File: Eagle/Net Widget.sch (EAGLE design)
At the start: 14 parts, among them IC1 ATmega1284P

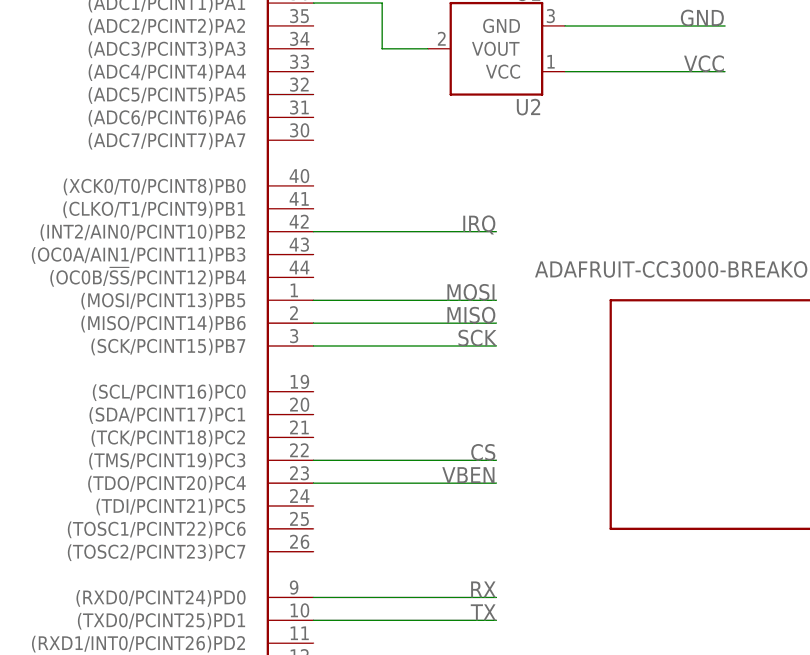
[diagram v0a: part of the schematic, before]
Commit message: Match CS and VBEN to Wicked Devices wildfire.
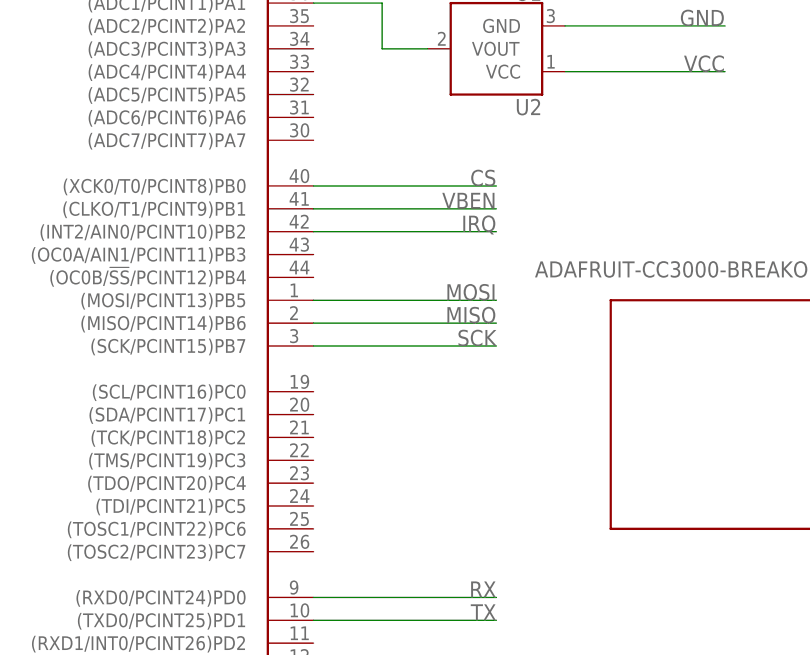
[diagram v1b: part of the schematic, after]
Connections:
- net CS: now also IC1.(XCK0/T0/PCINT8)PB0; no longer IC1.(TMS/PCINT19)PC3
- net VBEN: now also IC1.(CLKO/T1/PCINT9)PB1; no longer IC1.(TDO/PCINT20)PC4
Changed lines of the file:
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@@
 </segment>
 <segment>
-<pinref part="IC1" gate="G$1" pin="(TMS/PCINT19)PC3"/>
-<wire x1="83.82" y1="27.94" x2="104.14" y2="27.94" width="0.1524" layer="91"/>
-<label x="104.14" y="27.94" size="1.778" layer="95" rot="MR0"/>
+<pinref part="IC1" gate="G$1" pin="(XCK0/T0/PCINT8)PB0"/>
+<wire x1="83.82" y1="58.42" x2="104.14" y2="58.42" width="0.1524" layer="91"/>
+<label x="104.14" y="58.42" size="1.778" layer="95" rot="MR0"/>
 </segment>
 </net>
@@
 </segment>
 <segment>
-<pinref part="IC1" gate="G$1" pin="(TDO/PCINT20)PC4"/>
-<wire x1="83.82" y1="25.4" x2="104.14" y2="25.4" width="0.1524" layer="91"/>
-<label x="104.14" y="25.4" size="1.778" layer="95" rot="MR0"/>
+<pinref part="IC1" gate="G$1" pin="(CLKO/T1/PCINT9)PB1"/>
+<wire x1="83.82" y1="55.88" x2="104.14" y2="55.88" width="0.1524" layer="91"/>
+<label x="104.14" y="55.88" size="1.778" layer="95" rot="MR0"/>
 </segment>
 </net>

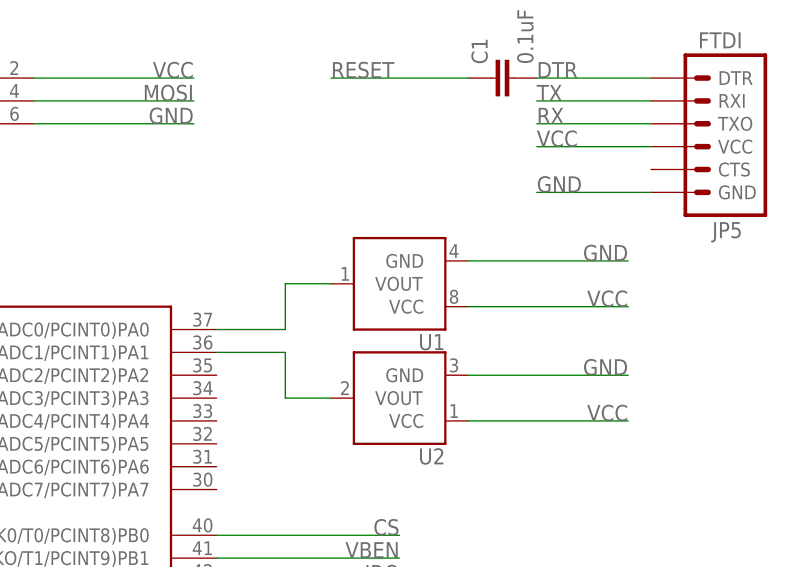
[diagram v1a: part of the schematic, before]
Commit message: Re-route w/ more space between pads and vias.
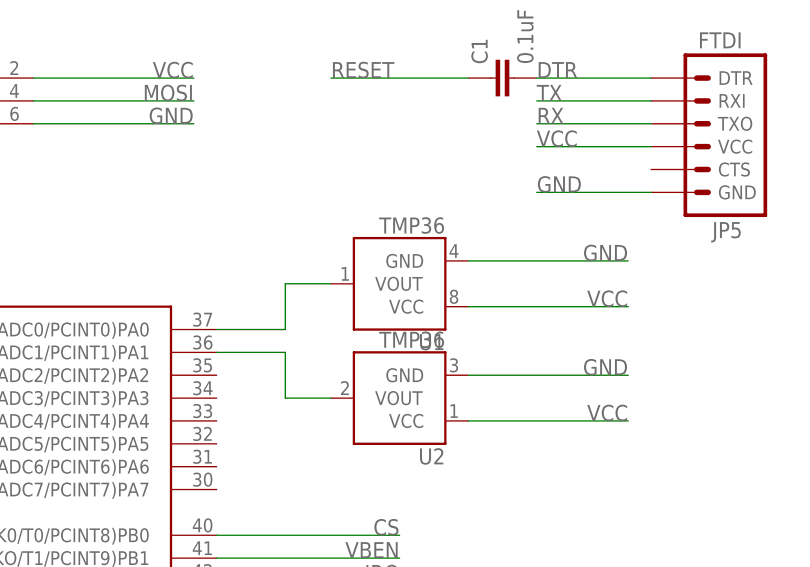
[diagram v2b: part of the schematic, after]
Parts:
- U1, U2: value (none) -> TMP36
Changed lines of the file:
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@@
 <part name="C1" library="rcl" deviceset="C-EU" device="C1206" value="0.1uF"/>
 <part name="CN1" library="Net Widget" deviceset="USB" device="PWR"/>
-<part name="U1" library="Net Widget" deviceset="TMP36" device=""/>
-<part name="U2" library="Net Widget" deviceset="TMP36" device="GT9"/>
+<part name="U1" library="Net Widget" deviceset="TMP36" device="" value="TMP36"/>
+<part name="U2" library="Net Widget" deviceset="TMP36" device="GT9" value="TMP36"/>
 </parts>
 <sheets>

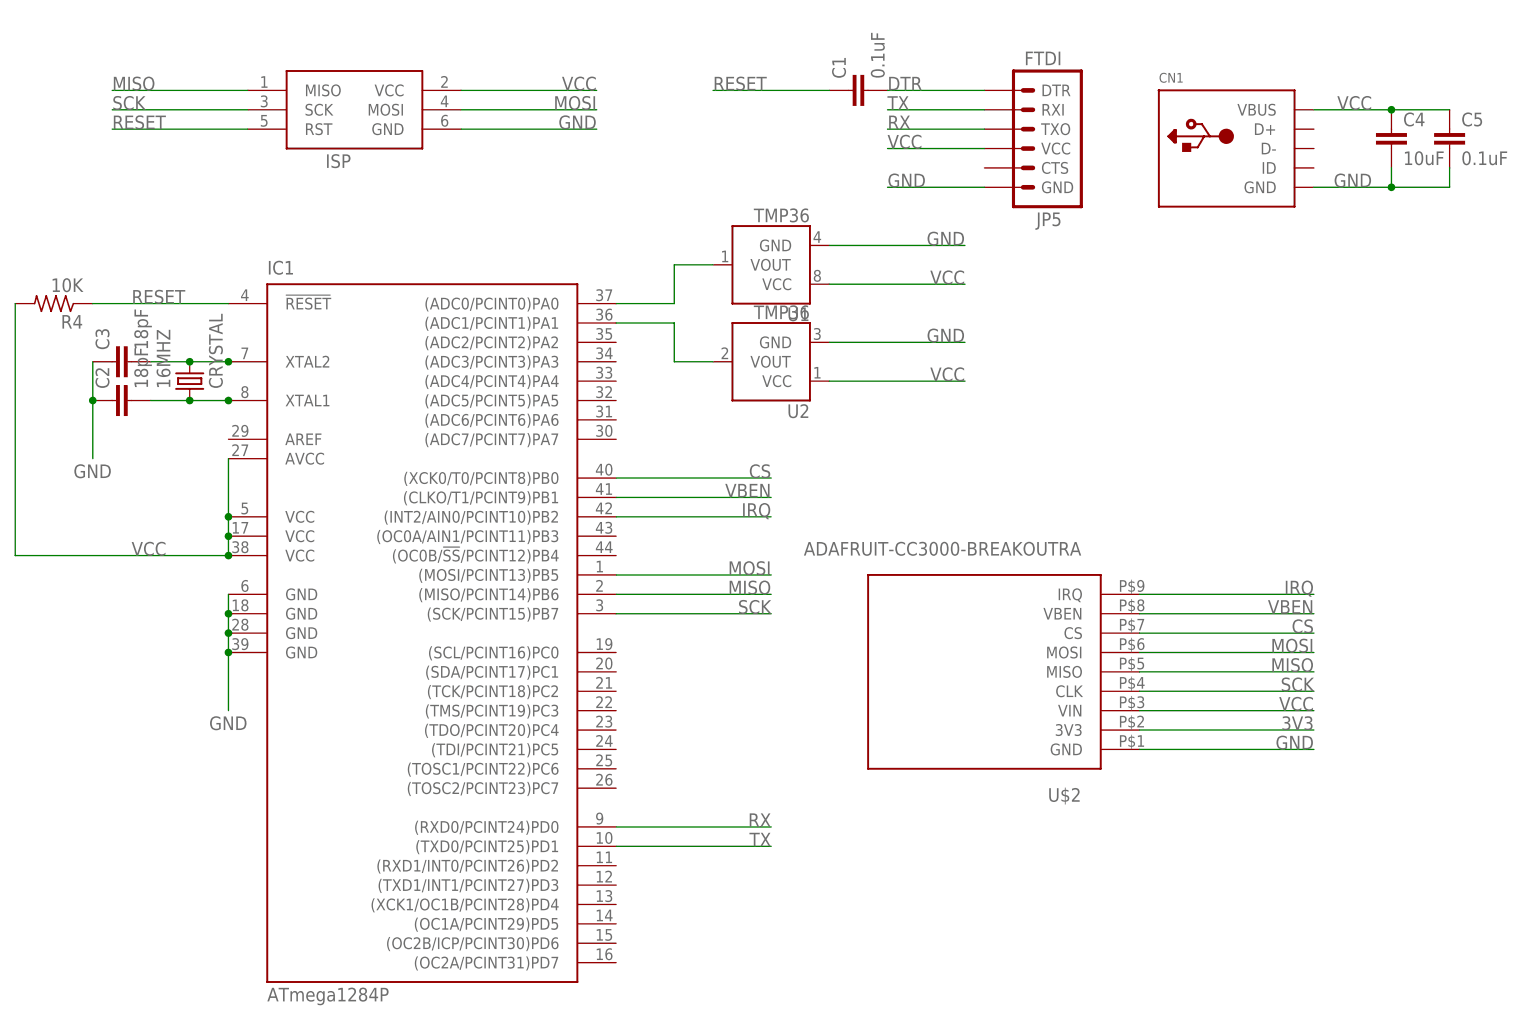
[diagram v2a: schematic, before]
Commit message: Remove temp sensor; add LEDs and touch.
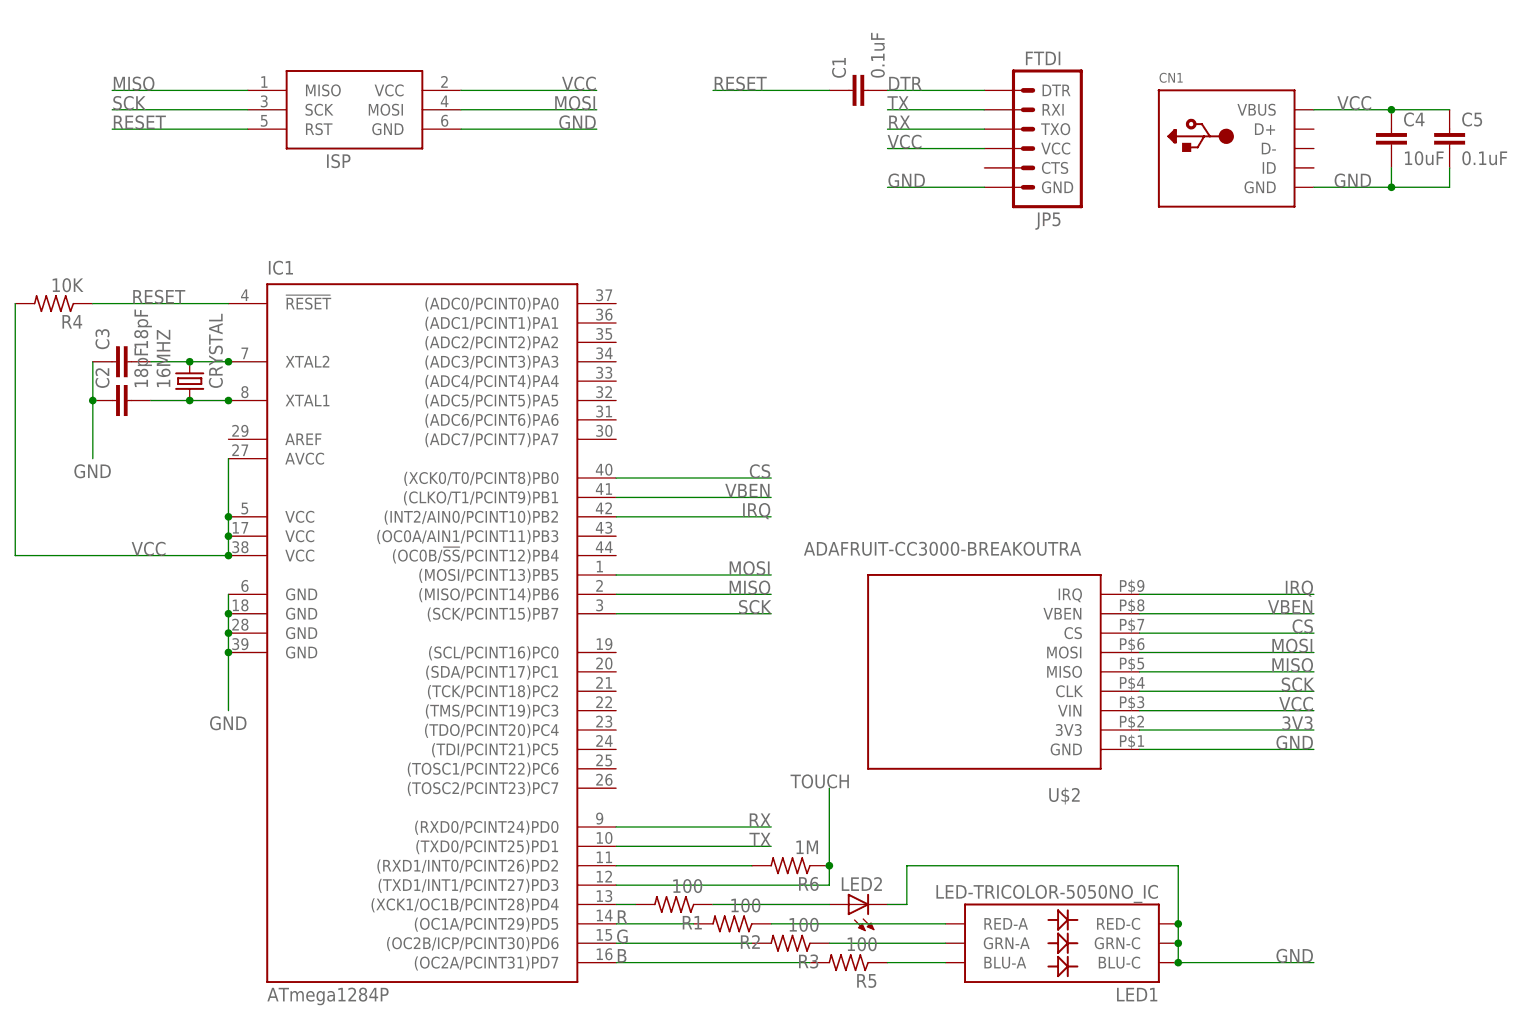
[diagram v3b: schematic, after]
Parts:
- removed U1: TMP36, Net Widget:TMP36
- removed U2: TMP36, Net Widget:TMP36GT9
- added LED1: LED-TRICOLOR-5050NO_IC, SparkFun-LED:LED-TRICOLOR-5050NO_IC
- added LED2: (no value), led:LEDSMT1206
- added R1, R2, R3, R5: 100, rcl:R-US_R1206
- added R6: 1M, rcl:R-US_R1206
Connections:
- removed net N$2: IC1.(ADC1/PCINT1)PA1, U2.VOUT
- new net B: IC1.(OC2A/PCINT31)PD7, R5.2
- new net G: IC1.(OC2B/ICP/PCINT30)PD6, R3.2
- new net N$10: LED1.RED-A, R2.1
- new net N$11: LED1.GRN-A, R3.1
- new net N$12: LED1.BLU-A, R5.1
- new net N$3: IC1.(XCK1/OC1B/PCINT28)PD4, R1.2
- new net N$9: LED2.A, R1.1
- new net R: IC1.(OC1A/PCINT29)PD5, R2.2
- new net TOUCH: IC1.(TXD1/INT1/PCINT27)PD3, R6.1
- net GND: now also LED1.BLU-C, LED1.GRN-C, LED1.RED-C, LED2.C; no longer U1.GND, U2.GND
- net N$1: now also IC1.(RXD1/INT0/PCINT26)PD2, R6.2; no longer IC1.(ADC0/PCINT0)PA0, U1.VOUT
- net VCC: no longer U1.VCC, U2.VCC
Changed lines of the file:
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@@
 <part name="C1" library="rcl" deviceset="C-EU" device="C1206" value="0.1uF"/>
 <part name="CN1" library="Net Widget" deviceset="USB" device="PWR"/>
-<part name="U1" library="Net Widget" deviceset="TMP36" device="" value="TMP36"/>
-<part name="U2" library="Net Widget" deviceset="TMP36" device="GT9" value="TMP36"/>
+<part name="LED1" library="SparkFun-LED" deviceset="LED-TRICOLOR-5050" device="NO_IC"/>
+<part name="LED2" library="led" deviceset="LED" device="SMT1206"/>
+<part name="R1" library="rcl" deviceset="R-US_" device="R1206" value="100"/>
+<part name="R2" library="rcl" deviceset="R-US_" device="R1206" value="100"/>
+<part name="R3" library="rcl" deviceset="R-US_" device="R1206" value="100"/>
+<part name="R5" library="rcl" deviceset="R-US_" device="R1206" value="100"/>
+<part name="R6" library="rcl" deviceset="R-US_" device="R1206" value="1M"/>
 </parts>
 <sheets>
@@
 <instance part="C1" gate="G$1" x="114.3" y="109.22" rot="R90"/>
 <instance part="CN1" gate="G$1" x="165.1" y="101.6"/>
-<instance part="U1" gate="G$1" x="104.14" y="86.36" rot="R180"/>
-<instance part="U2" gate="G$1" x="104.14" y="73.66" rot="R180"/>
+<instance part="LED1" gate="D1" x="142.24" y="-2.54" rot="R180"/>
+<instance part="LED2" gate="G$1" x="114.3" y="2.54" rot="R90"/>
+<instance part="R1" gate="G$1" x="91.44" y="2.54" rot="R180"/>
+<instance part="R2" gate="G$1" x="99.06" y="0" rot="R180"/>
+<instance part="R3" gate="G$1" x="106.68" y="-2.54" rot="R180"/>
+<instance part="R5" gate="G$1" x="114.3" y="-5.08" rot="R180"/>
+<instance part="R6" gate="G$1" x="106.68" y="7.62" rot="R180"/>
 </instances>
 <busses>
@@
 </segment>
 <segment>
-<pinref part="U1" gate="G$1" pin="GND"/>
-<wire x1="111.76" y1="88.9" x2="129.54" y2="88.9" width="0.1524" layer="91"/>
-<label x="129.54" y="88.9" size="1.778" layer="95" rot="MR0"/>
-</segment>
-<segment>
-<pinref part="U2" gate="G$1" pin="GND"/>
-<wire x1="111.76" y1="76.2" x2="129.54" y2="76.2" width="0.1524" layer="91"/>
-<label x="129.54" y="76.2" size="1.778" layer="95" rot="MR0"/>
+<pinref part="LED1" gate="D1" pin="BLU-C"/>
+<pinref part="LED1" gate="D1" pin="GRN-C"/>
+<wire x1="157.48" y1="-5.08" x2="157.48" y2="-2.54" width="0.1524" layer="91"/>
+<pinref part="LED1" gate="D1" pin="RED-C"/>
+<wire x1="157.48" y1="-2.54" x2="157.48" y2="0" width="0.1524" layer="91"/>
+<junction x="157.48" y="-2.54"/>
+<junction x="157.48" y="0"/>
+<label x="175.26" y="-5.08" size="1.778" layer="95" rot="MR0"/>
+<wire x1="157.48" y1="-5.08" x2="175.26" y2="-5.08" width="0.1524" layer="91"/>
+<junction x="157.48" y="-5.08"/>
+<pinref part="LED2" gate="G$1" pin="C"/>
+<wire x1="119.38" y1="2.54" x2="121.92" y2="2.54" width="0.1524" layer="91"/>
+<wire x1="121.92" y1="2.54" x2="121.92" y2="7.62" width="0.1524" layer="91"/>
+<wire x1="121.92" y1="7.62" x2="157.48" y2="7.62" width="0.1524" layer="91"/>
+<wire x1="157.48" y1="7.62" x2="157.48" y2="0" width="0.1524" layer="91"/>
 </segment>
 </net>
@@
 <label x="119.38" y="101.6" size="1.778" layer="95"/>
 </segment>
-<segment>
-<pinref part="U1" gate="G$1" pin="VCC"/>
-<wire x1="111.76" y1="83.82" x2="129.54" y2="83.82" width="0.1524" layer="91"/>
-<label x="129.54" y="83.82" size="1.778" layer="95" rot="MR0"/>
-</segment>
-<segment>
-<pinref part="U2" gate="G$1" pin="VCC"/>
-<wire x1="111.76" y1="71.12" x2="129.54" y2="71.12" width="0.1524" layer="91"/>
-<label x="129.54" y="71.12" size="1.778" layer="95" rot="MR0"/>
-</segment>
 </net>
 <net name="RESET" class="0">
@@
 </segment>
 </net>
+<net name="N$3" class="0">
+<segment>
+<pinref part="IC1" gate="G$1" pin="(XCK1/OC1B/PCINT28)PD4"/>
+<pinref part="R1" gate="G$1" pin="2"/>
+<wire x1="86.36" y1="2.54" x2="83.82" y2="2.54" width="0.1524" layer="91"/>
+</segment>
+</net>
+<net name="R" class="0">
+<segment>
+<pinref part="IC1" gate="G$1" pin="(OC1A/PCINT29)PD5"/>
+<pinref part="R2" gate="G$1" pin="2"/>
+<wire x1="93.98" y1="0" x2="83.82" y2="0" width="0.1524" layer="91"/>
+<label x="83.82" y="0" size="1.778" layer="95"/>
+</segment>
+</net>
+<net name="G" class="0">
+<segment>
+<pinref part="IC1" gate="G$1" pin="(OC2B/ICP/PCINT30)PD6"/>
+<pinref part="R3" gate="G$1" pin="2"/>
+<wire x1="101.6" y1="-2.54" x2="83.82" y2="-2.54" width="0.1524" layer="91"/>
+<label x="83.82" y="-2.54" size="1.778" layer="95"/>
+</segment>
+</net>
+<net name="B" class="0">
+<segment>
+<pinref part="IC1" gate="G$1" pin="(OC2A/PCINT31)PD7"/>
+<pinref part="R5" gate="G$1" pin="2"/>
+<wire x1="109.22" y1="-5.08" x2="83.82" y2="-5.08" width="0.1524" layer="91"/>
+<label x="83.82" y="-5.08" size="1.778" layer="95"/>
+</segment>
+</net>
+<net name="N$9" class="0">
+<segment>
+<pinref part="R1" gate="G$1" pin="1"/>
+<pinref part="LED2" gate="G$1" pin="A"/>
+<wire x1="111.76" y1="2.54" x2="96.52" y2="2.54" width="0.1524" layer="91"/>
+</segment>
+</net>
+<net name="N$10" class="0">
+<segment>
+<pinref part="R2" gate="G$1" pin="1"/>
+<pinref part="LED1" gate="D1" pin="RED-A"/>
+<wire x1="127" y1="0" x2="104.14" y2="0" width="0.1524" layer="91"/>
+</segment>
+</net>
+<net name="N$11" class="0">
+<segment>
+<pinref part="R3" gate="G$1" pin="1"/>
+<pinref part="LED1" gate="D1" pin="GRN-A"/>
+<wire x1="127" y1="-2.54" x2="111.76" y2="-2.54" width="0.1524" layer="91"/>
+</segment>
+</net>
+<net name="N$12" class="0">
+<segment>
+<pinref part="R5" gate="G$1" pin="1"/>
+<pinref part="LED1" gate="D1" pin="BLU-A"/>
+<wire x1="127" y1="-5.08" x2="119.38" y2="-5.08" width="0.1524" layer="91"/>
+</segment>
+</net>
 <net name="N$1" class="0">
 <segment>
-<pinref part="U1" gate="G$1" pin="VOUT"/>
-<wire x1="96.52" y1="86.36" x2="91.44" y2="86.36" width="0.1524" layer="91"/>
-<wire x1="91.44" y1="86.36" x2="91.44" y2="81.28" width="0.1524" layer="91"/>
-<pinref part="IC1" gate="G$1" pin="(ADC0/PCINT0)PA0"/>
-<wire x1="91.44" y1="81.28" x2="83.82" y2="81.28" width="0.1524" layer="91"/>
-</segment>
-</net>
-<net name="N$2" class="0">
-<segment>
-<pinref part="U2" gate="G$1" pin="VOUT"/>
-<wire x1="96.52" y1="73.66" x2="91.44" y2="73.66" width="0.1524" layer="91"/>
-<wire x1="91.44" y1="73.66" x2="91.44" y2="78.74" width="0.1524" layer="91"/>
-<pinref part="IC1" gate="G$1" pin="(ADC1/PCINT1)PA1"/>
-<wire x1="91.44" y1="78.74" x2="83.82" y2="78.74" width="0.1524" layer="91"/>
-</segment>
-</net>
+<pinref part="IC1" gate="G$1" pin="(RXD1/INT0/PCINT26)PD2"/>
+<pinref part="R6" gate="G$1" pin="2"/>
+<wire x1="101.6" y1="7.62" x2="83.82" y2="7.62" width="0.1524" layer="91"/>
+</segment>
+</net>
+<net name="TOUCH" class="0">
+<segment>
+<pinref part="IC1" gate="G$1" pin="(TXD1/INT1/PCINT27)PD3"/>
+<pinref part="R6" gate="G$1" pin="1"/>
+<wire x1="83.82" y1="5.08" x2="111.76" y2="5.08" width="0.1524" layer="91"/>
+<wire x1="111.76" y1="5.08" x2="111.76" y2="7.62" width="0.1524" layer="91"/>
+<wire x1="111.76" y1="7.62" x2="111.76" y2="17.78" width="0.1524" layer="91"/>
+<junction x="111.76" y="7.62"/>
+<label x="106.68" y="17.78" size="1.778" layer="95"/>
+</segment>
+</net>
